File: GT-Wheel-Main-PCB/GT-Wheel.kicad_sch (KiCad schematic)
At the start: 69 parts, among them J2 TC2050, J3 0532610471, J4 USB_A, J5 0532610871, J6 0532610871, U1 STM32F303RETx, U2 USB2512B, U3 AP2112K-3.3, X1 8MHz, X2 24MHz

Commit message: updating PCB
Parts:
- removed C1, C11, C12, C13, C14, C15, C16, C17, C18, C2, C3, C4, C47, C5, C53, C54, C8: 100nF-CER-25V-0402, Capacitor_SMD:C_0402_1005Metric, symbol CAP-SMD-25V:100nF-CER-25V-0402
- removed C10, C9: 10uF-CER-25V-0805, Capacitor_SMD:C_0805_2012Metric, symbol CAP-SMD-25V:10uF-CER-25V-0805
- removed C19, C20: ~, Capacitor_SMD:C_0402_1005Metric, symbol CAP-SMD-50V:18pF-CER-50V-0402
- removed C48, C49, C50, C51: ${SIM.PARAMS}, Capacitor_SMD:C_0805_2012Metric, symbol CAP-SMD-25V:1uF-CER-25V-0805
- removed C52: ${SIM.PARAMS}, Capacitor_SMD:C_0805_2012Metric, symbol CAP-SMD-16V:4.7uF-CER-16V-0805
- removed C55: ${SIM.PARAMS}, Capacitor_SMD:CP_Elec_6.3x5.9, symbol CAP-SMD-25V:100uF-ELEC-50V-RAD6.3Dx6H
- removed C6, C7: ~, Capacitor_SMD:C_0402_1005Metric, symbol CAP-SMD-50V:20pF-CER-50V-0402
- removed J2: TC2050, Connector:Tag-Connect_TC2050-IDC-FP_2x05_P1.27mm_Vertical, symbol CONN-TAG-CONNECT:TC2050
- removed J4: USB_A, CONN-USB:GSB12121RSKHR, symbol Connector:USB_A
- removed R1, R13, R14, R15, R16, R17, R18, R3: 100kR-SMD-100mW-0603, Resistor_SMD:R_0603_1608Metric, symbol RES-SMD-100mW:100kR-SMD-100mW-0603
- removed R19: ${SIM.PARAMS}, Resistor_SMD:R_0603_1608Metric, symbol RES-SMD-100mW:49K9R-SMD-100mW-0603
- removed R2: 10kR-SMD-100mW-0603, Resistor_SMD:R_0603_1608Metric, symbol RES-SMD-100mW:10kR-SMD-100mW-0603
- removed R4: 12kR-SMD-100mW-0603, Resistor_SMD:R_0603_1608Metric, symbol RES-SMD-100mW:12kR-SMD-100mW-0603
- removed U1: STM32F303RETx, Package_QFP:LQFP-64_10x10mm_P0.5mm, symbol MCU_ST_STM32F3:STM32F303RETx
- removed U2: USB2512B, Package_DFN_QFN:QFN-36-1EP_6x6mm_P0.5mm_EP3.7x3.7mm_ThermalVias, symbol IC-SMD-USB-HUB:USB2512B
- removed U3: AP2112K-3.3, Package_TO_SOT_SMD:SOT-23-5, symbol Regulator_Linear:AP2112K-3.3
- removed U4: ~, SOT-SMD:SOT-23-6, symbol IC-SMD-LOAD-SW:AP22653W6-7
- removed X1: 8MHz, Crystal:Crystal_SMD_EuroQuartz_MT-4Pin_3.2x2.5mm, symbol XTAL:XTAL_8MHz_12pF
- removed X2: 24MHz, Crystal:Crystal_SMD_EuroQuartz_MT-4Pin_3.2x2.5mm, symbol XTAL:XTAL_24MHz_6pF
- added U1: ATmega2560-16A, Package_QFP:TQFP-100_14x14mm_P0.5mm, symbol MCU_Microchip_ATmega:ATmega2560-16A
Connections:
- net USB_D+: no longer names the net of L1.2
- net USB_D-: no longer names the net of L1.3
- new net: U1.10 (VCC), U1.31 (VCC), U1.61 (VCC), U1.80 (VCC)
- new net: U1.11 (GND), U1.32 (GND), U1.62 (GND), U1.81 (GND), U1.99 (GND)
- no-connect marks 15 -> 0
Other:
- moved on the sheet: D1, D2, D3, J3, J5, J6, L1, LF1, LF2, WP1, WP10, WP11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

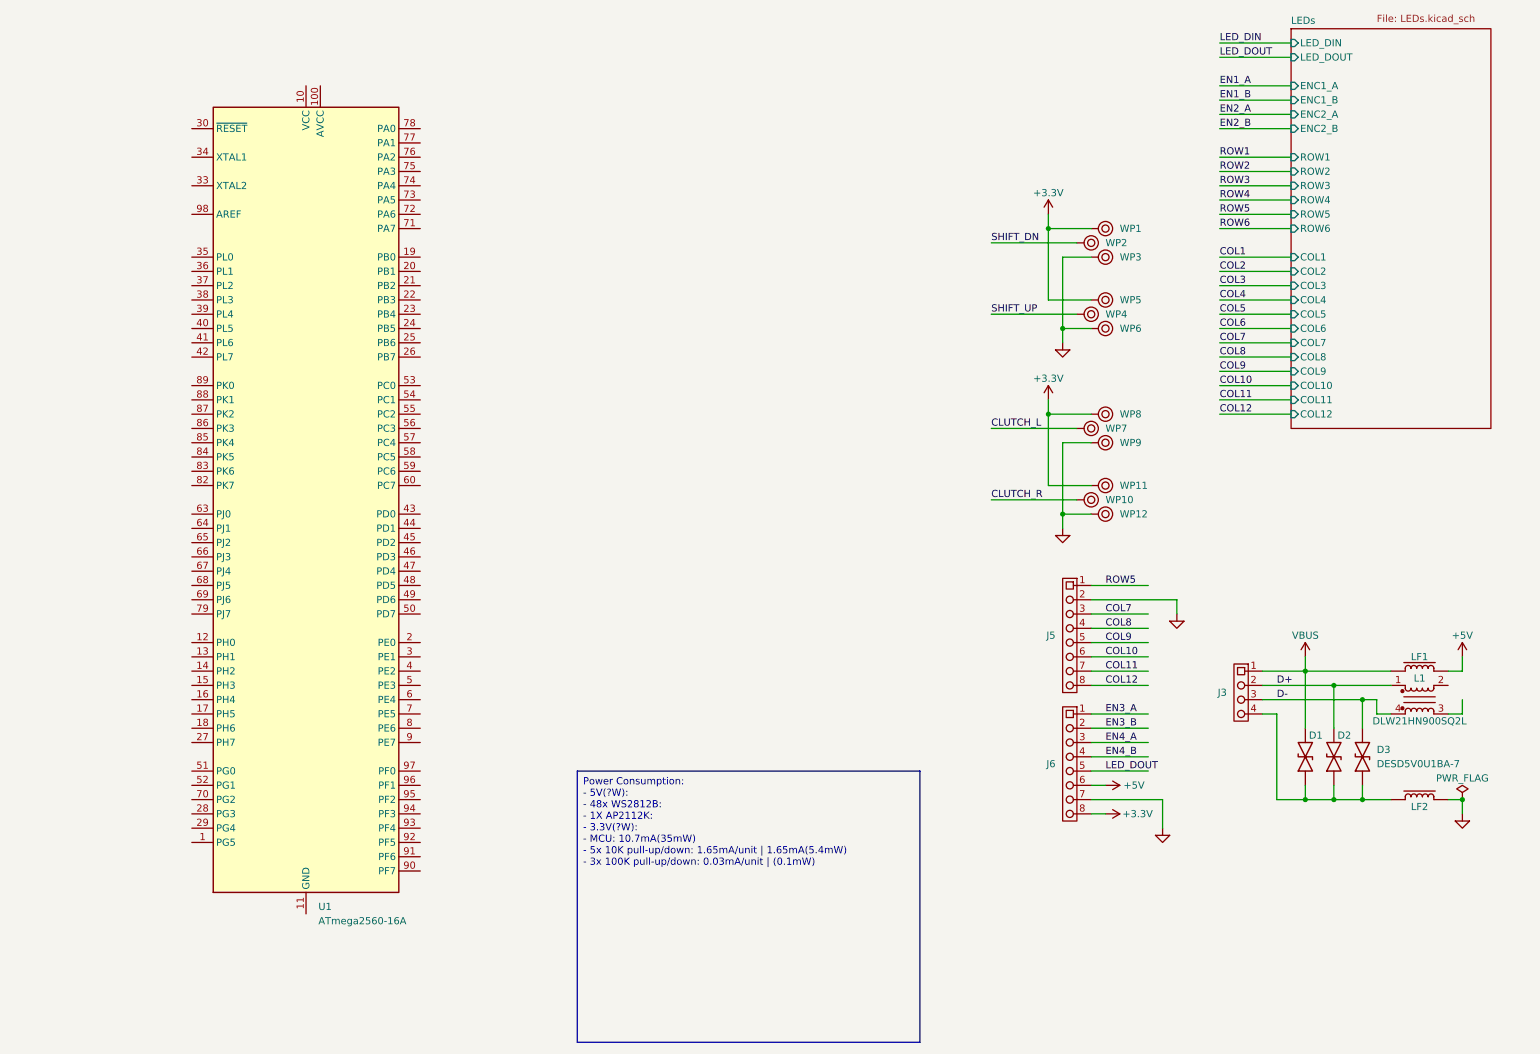
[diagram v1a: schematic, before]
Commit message: reverting to stm32
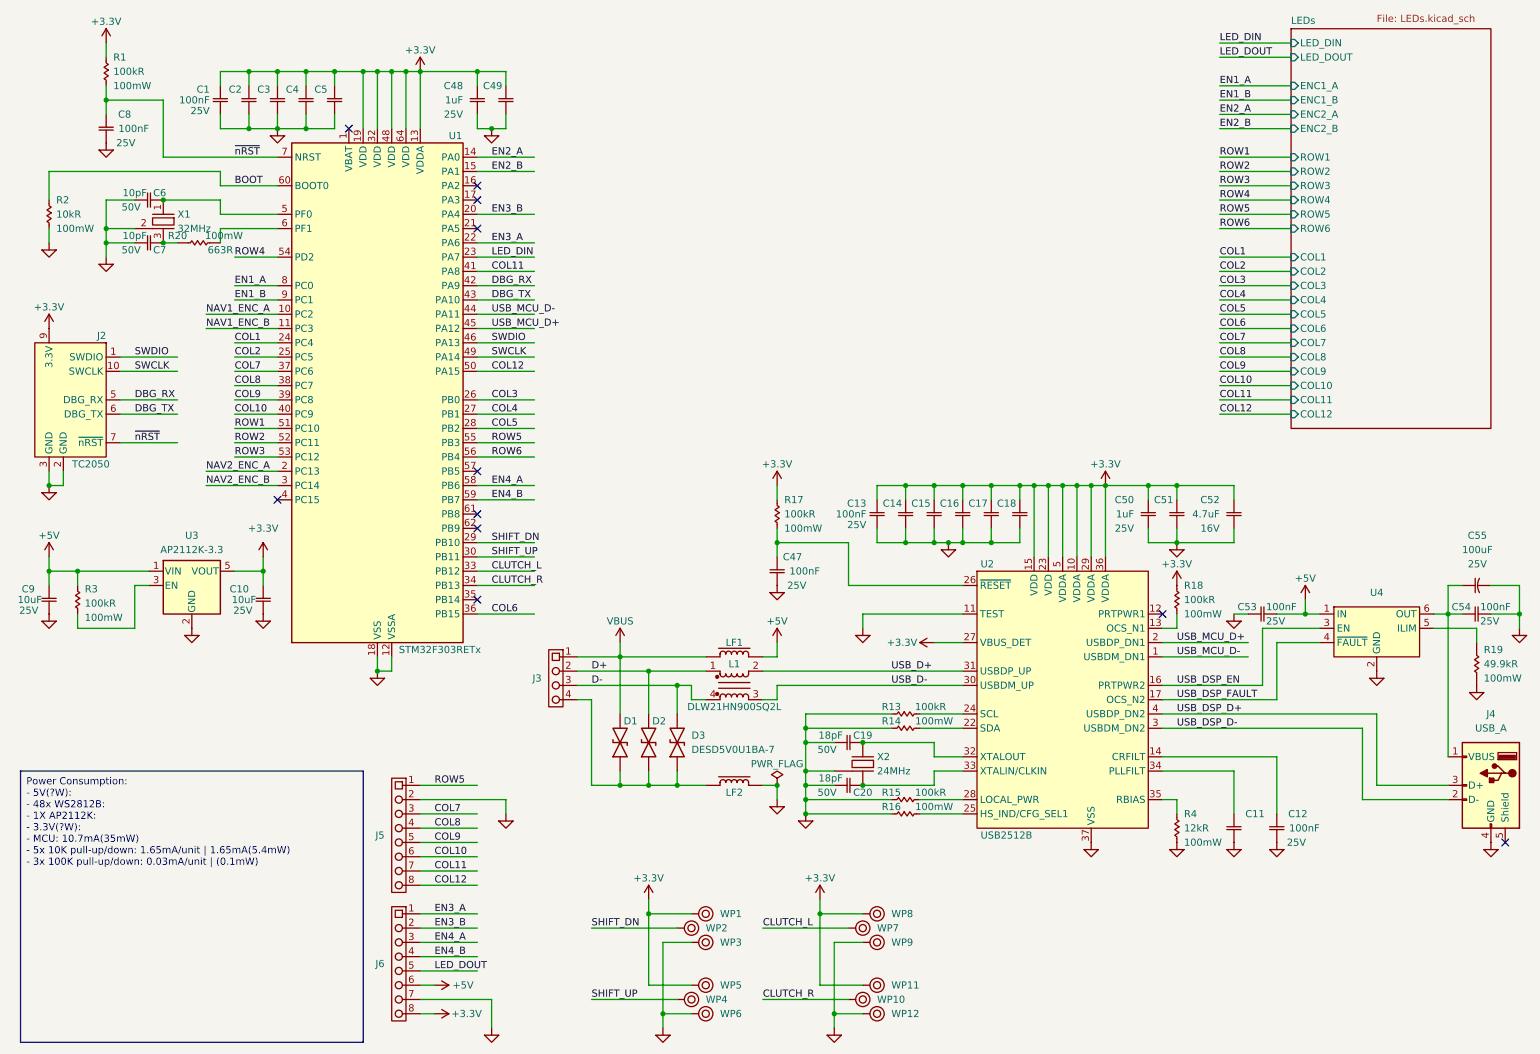
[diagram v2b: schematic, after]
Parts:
- removed U1: ATmega2560-16A, Package_QFP:TQFP-100_14x14mm_P0.5mm, symbol MCU_Microchip_ATmega:ATmega2560-16A
- added C1, C11, C12, C13, C14, C15, C16, C17, C18, C2, C3, C4, C47, C5, C53, C54, C8: 100nF-CER-25V-0402, Capacitor_SMD:C_0402_1005Metric, symbol CAP-SMD-25V:100nF-CER-25V-0402
- added C10, C9: 10uF-CER-25V-0805, Capacitor_SMD:C_0805_2012Metric, symbol CAP-SMD-25V:10uF-CER-25V-0805
- added C19, C20: ~, Capacitor_SMD:C_0402_1005Metric, symbol CAP-SMD-50V:18pF-CER-50V-0402
- added C48, C49, C50, C51: ${SIM.PARAMS}, Capacitor_SMD:C_0805_2012Metric, symbol CAP-SMD-25V:1uF-CER-25V-0805
- added C52: ${SIM.PARAMS}, Capacitor_SMD:C_0805_2012Metric, symbol CAP-SMD-16V:4.7uF-CER-16V-0805
- added C55: ${SIM.PARAMS}, Capacitor_SMD:CP_Elec_6.3x5.9, symbol CAP-SMD-25V:100uF-ELEC-50V-RAD6.3Dx6H
- added C6, C7: ~, Capacitor_SMD:C_0201_0603Metric, symbol CAP-SMD-50V:10pF-CER-50V-0603
- added J2: TC2050, Connector:Tag-Connect_TC2050-IDC-FP_2x05_P1.27mm_Vertical, symbol CONN-TAG-CONNECT:TC2050
- added J4: USB_A, CONN-USB:GSB12121RSKHR, symbol Connector:USB_A
- added R1, R13, R14, R15, R16, R17, R18, R3: 100kR-SMD-100mW-0603, Resistor_SMD:R_0603_1608Metric, symbol RES-SMD-100mW:100kR-SMD-100mW-0603
- added R19: ${SIM.PARAMS}, Resistor_SMD:R_0603_1608Metric, symbol RES-SMD-100mW:49K9R-SMD-100mW-0603
- added R2: 10kR-SMD-100mW-0603, Resistor_SMD:R_0603_1608Metric, symbol RES-SMD-100mW:10kR-SMD-100mW-0603
- added R20: ${SIM.PARAMS}, Resistor_SMD:R_0603_1608Metric, symbol RES-SMD-100mW:663R-SMD-100mW-0603
- added R4: 12kR-SMD-100mW-0603, Resistor_SMD:R_0603_1608Metric, symbol RES-SMD-100mW:12kR-SMD-100mW-0603
- added U1: STM32F303RETx, Package_QFP:LQFP-64_10x10mm_P0.5mm, symbol MCU_ST_STM32F3:STM32F303RETx
- added U2: USB2512B, Package_DFN_QFN:QFN-36-1EP_6x6mm_P0.5mm_EP3.7x3.7mm_ThermalVias, symbol IC-SMD-USB-HUB:USB2512B
- added U3: AP2112K-3.3, Package_TO_SOT_SMD:SOT-23-5, symbol Regulator_Linear:AP2112K-3.3
- added U4: ~, SOT-SMD:SOT-23-6, symbol IC-SMD-LOAD-SW:AP22653W6-7
- added X1: 32MHz, Crystal:Crystal_SMD_EuroQuartz_X22-4Pin_2.5x2.0mm, symbol XTAL:XTAL_32MHz_10pF
- added X2: 24MHz, Crystal:Crystal_SMD_EuroQuartz_MT-4Pin_3.2x2.5mm, symbol XTAL:XTAL_24MHz_6pF
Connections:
- net CLUTCH_L: now also U1.33 (PB12)
- net CLUTCH_R: now also U1.34 (PB13)
- net COL1: now also U1.24 (PC4)
- net COL10: now also U1.40 (PC9)
- net COL11: now also U1.41 (PA8)
- net COL12: now also U1.50 (PA15)
- net COL2: now also U1.25 (PC5)
- net COL3: now also U1.26 (PB0)
- net COL4: now also U1.27 (PB1)
- net COL5: now also U1.28 (PB2)
- net COL6: now also U1.36 (PB15)
- net COL7: now also U1.37 (PC6)
- net COL8: now also U1.38 (PC7)
- net COL9: now also U1.39 (PC8)
- net EN1_A: now also U1.8 (PC0)
- net EN1_B: now also U1.9 (PC1)
- net EN2_A: now also U1.14 (PA0)
- net EN2_B: now also U1.15 (PA1)
- net EN3_A: now also U1.22 (PA6)
- net EN3_B: now also U1.20 (PA4)
- net EN4_A: now also U1.58 (PB6)
- net EN4_B: now also U1.59 (PB7)
- net LED_DIN: now also U1.23 (PA7)
- net LOGIC_GND: now also C1.2, C10.2, C11.2, C12.2, C13.2, C14.2, C15.2, C16.2, C17.2, C18.2, C19.1, C2.2, C20.1, C3.2, C4.2, C47.2, C48.2, C49.2, C5.2, C50.2, C51.2, C52.2, C53.1, C54.2, C55.2, C6.1, C7.1, C8.2, C9.2, J2.2 (GND), J2.3 (GND), J4.4 (GND), R13.1, R14.1, R15.1, R16.1, R19.2, R2.2, R4.2, U1.12 (VSSA), U1.18 (VSS), U1.31 (VSS), U1.47 (VSS), U1.63 (VSS), U2.11 (TEST), U2.37 (VSS), U3.2 (GND), U4.2 (GND), X1.2, X1.4, X2.2, X2.4
- net ROW1: now also U1.51 (PC10)
- net ROW2: now also U1.52 (PC11)
- net ROW3: now also U1.53 (PC12)
- net ROW4: now also U1.54 (PD2)
- net ROW5: now also U1.55 (PB3)
- net ROW6: now also U1.56 (PB4)
- net SHIFT_DN: now also U1.29 (PB10)
- net SHIFT_UP: now also U1.30 (PB11)
- net USB_D+: now reaches L1.2
- net USB_D+: now also U2.31 (USBDP_UP)
- net USB_D-: now reaches L1.3
- net USB_D-: now also U2.30 (USBDM_UP)
- new net: C54.1, C55.1, J4.1 (VBUS), U4.6 (OUT)
- new net: C9.1, R3.1, U3.1 (VIN)
- new net: R3.2, U3.3 (EN)
- new net: C13.1, C14.1, C15.1, C16.1, C17.1, C18.1, C50.1, C51.1, C52.1, U2.10 (VDDA), U2.15 (VDD), U2.23 (VDD), U2.29 (VDDA), U2.36 (VDDA), U2.5 (VDDA)
- new net: C1.1, C2.1, C3.1, C4.1, C48.1, C49.1, C5.1, U1.13 (VDDA), U1.19 (VDD), U1.32 (VDD), U1.48 (VDD), U1.64 (VDD)
- new net: C53.2, U4.1 (IN)
- new net: R19.1, U4.5 (ILIM)
- new net: C6.2, U1.5 (PF0), X1.1
- new net: R20.2, U1.6 (PF1)
- new net: C47.1, R17.2, U2.26 (~{RESET})
- new net: C19.2, U2.32 (XTALOUT), X2.1
- new net: C7.2, R20.1, X1.3
- new net: R18.2, U2.13 (OCS_N1)
- new net: C20.2, U2.33 (XTALIN/CLKIN), X2.3
- new net: R13.2, U2.24 (SCL)
- new net: C12.1, U2.14 (CRFILT)
- new net: R14.2, U2.22 (SDA)
- new net: R16.2, U2.25 (HS_IND/CFG_SEL1)
- new net: R15.2, U2.28 (LOCAL_PWR)
- new net: C11.1, U2.34 (PLLFILT)
- new net: R4.1, U2.35 (RBIAS)
- new net +3.3V: C10.1, U3.5 (VOUT)
- new net BOOT: R2.1, U1.60 (BOOT0)
- new net DBG_RX: J2.5 (DBG_RX), U1.42 (PA9)
- new net DBG_TX: J2.6 (DBG_TX), U1.43 (PA10)
- new net NAV1_ENC_A: U1.10 (PC2)
- new net NAV1_ENC_B: U1.11 (PC3)
- new net NAV2_ENC_A: U1.2 (PC13)
- new net NAV2_ENC_B: U1.3 (PC14)
- new net SWCLK: J2.10 (SWCLK), U1.49 (PA14)
- new net SWDIO: J2.1 (SWDIO), U1.46 (PA13)
- new net USB_DSP_D+: J4.3 (D+), U2.4 (USBDP_DN2)
- new net USB_DSP_D-: J4.2 (D-), U2.3 (USBDM_DN2)
- new net USB_DSP_EN: U2.16 (PRTPWR2), U4.3 (EN)
- new net USB_DSP_FAULT: U2.17 (OCS_N2), U4.4 (~{FAULT})
- new net USB_MCU_D+: U1.45 (PA12), U2.2 (USBDP_DN1)
- new net USB_MCU_D-: U1.44 (PA11), U2.1 (USBDM_DN1)
- new net ~{nRST}: C8.1, J2.7 (~{nRST}), R1.2, U1.7 (NRST)
- no-connect marks 0 -> 11
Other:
- moved on the sheet: D1, D2, D3, J3, J5, J6, L1, LF1, LF2, WP1, WP10, WP11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

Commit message: removing usb hub
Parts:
- removed C11, C12, C13, C14, C15, C16, C17, C18, C47, C53, C54: 100nF-CER-25V-0402, Capacitor_SMD:C_0402_1005Metric, symbol CAP-SMD-25V:100nF-CER-25V-0402
- removed C19, C20: ~, Capacitor_SMD:C_0402_1005Metric, symbol CAP-SMD-50V:18pF-CER-50V-0402
- removed C50, C51: ${SIM.PARAMS}, Capacitor_SMD:C_0805_2012Metric, symbol CAP-SMD-25V:1uF-CER-25V-0805
- removed C52: ${SIM.PARAMS}, Capacitor_SMD:C_0805_2012Metric, symbol CAP-SMD-16V:4.7uF-CER-16V-0805
- removed C55: ${SIM.PARAMS}, Capacitor_SMD:CP_Elec_6.3x5.9, symbol CAP-SMD-25V:100uF-ELEC-50V-RAD6.3Dx6H
- removed J4: USB_A, CONN-USB:GSB12121RSKHR, symbol Connector:USB_A
- removed R13, R14, R15, R16, R17, R18: 100kR-SMD-100mW-0603, Resistor_SMD:R_0603_1608Metric, symbol RES-SMD-100mW:100kR-SMD-100mW-0603
- removed R19: ${SIM.PARAMS}, Resistor_SMD:R_0603_1608Metric, symbol RES-SMD-100mW:49K9R-SMD-100mW-0603
- removed R4: 12kR-SMD-100mW-0603, Resistor_SMD:R_0603_1608Metric, symbol RES-SMD-100mW:12kR-SMD-100mW-0603
- removed U2: USB2512B, Package_DFN_QFN:QFN-36-1EP_6x6mm_P0.5mm_EP3.7x3.7mm_ThermalVias, symbol IC-SMD-USB-HUB:USB2512B
- removed U4: ~, SOT-SMD:SOT-23-6, symbol IC-SMD-LOAD-SW:AP22653W6-7
- removed X2: 24MHz, Crystal:Crystal_SMD_EuroQuartz_MT-4Pin_3.2x2.5mm, symbol XTAL:XTAL_24MHz_6pF
- added C64, C65, C66, C67: 100nF-CER-25V-0402, Capacitor_SMD:C_0402_1005Metric, symbol CAP-SMD-25V:100nF-CER-25V-0402
- added D14 (x2): BAT43W-TP, Diode_SMD:D_SOD-123, symbol DIODE-SMD-SCHOTTKY:BAT43W-TP
- added R37, R38, R39, R40, R41, R42, R43, R44: 10kR-SMD-100mW-0603, Resistor_SMD:R_0603_1608Metric, symbol RES-SMD-100mW:10kR-SMD-100mW-0603
- added SW7, SW8: ~, SWITCH-THT-FUNKY:RKJXT1F42001, symbol SWITCH-THT-FUNKY:RKJXT1F42001
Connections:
- net USB_D+ is gone; now on net USB_MCU_D+: L1.2
- net USB_D- is gone; now on net USB_MCU_D-: L1.3
- net COL1: now also J5.5, SW7.1 (A), SW8.1 (A)
- net COL2: now also J5.6, SW7.2 (B), SW8.2 (B)
- net COL3: now also J5.7, U1.37 (PC6), SW7.3 (C), SW8.3 (C); no longer U1.26 (PB0)
- net COL4: now also U1.38 (PC7), SW7.4 (D), SW8.4 (D); no longer U1.27 (PB1)
- net LOGIC_GND: now also J5.4, J5.8, C64.2, C65.2, C66.2, C67.2, SW7.10 (GND), SW7.9 (ENC_C), SW8.10 (GND), SW8.9 (ENC_C); no longer J5.2
- net NAV1_ENC_A: now also C65.1, R37.1
- net NAV1_ENC_B: now also C64.1, R38.1
- net NAV2_ENC_A: now also C67.1, R41.1
- net NAV2_ENC_B: now also C66.1, R42.1
- net ROW1: now also U1.39 (PC8); no longer U1.51 (PC10)
- net ROW2: now also U1.40 (PC9); no longer U1.52 (PC11)
- net ROW3: now also U1.51 (PC10); no longer U1.53 (PC12)
- net ROW4: now also J5.2, U1.52 (PC11)
- net ROW5: now also J5.3, U1.53 (PC12); no longer J5.1, U1.55 (PB3)
- net ROW6: now also U1.26 (PB0), D14.2 (A); no longer U1.56 (PB4)
- net EN8_A: now reaches U1.35 (PB14)
- net EN6_B: now reaches U1.57 (PB5)
- net EN7_A: now reaches U1.61 (PB8)
- net EN7_B: now reaches U1.62 (PB9)
- removed net COL10: J5.6, U1.40 (PC9)
- net COL11: no longer names the net of U1.41 (PA8)
- net COL11: no longer J5.7
- net COL12: no longer names the net of U1.50 (PA15)
- net COL12: no longer J5.8
- net COL5 renamed EN5_A
- net COL6 renamed EN8_B
- removed net COL7: J5.3, U1.37 (PC6)
- removed net COL8: J5.4, U1.38 (PC7)
- removed net COL9: J5.5, U1.39 (PC8)
- new net: R39.1, R40.1
- new net: R38.2, R39.2, SW7.8 (ENC_B)
- new net: R42.2, R43.2, SW8.8 (ENC_B)
- new net: R37.2, R40.2, SW7.7 (ENC_A)
- new net: R41.2, R44.2, SW8.7 (ENC_A)
- new net: R43.1, R44.1
- new net: D14.1 (K), SW8.6 (COM)
- new net: D14.1 (K), SW7.6 (COM)
- new net EN5_B: U1.55 (PB3)
- new net EN6_A: U1.56 (PB4)
- new net ROW7: D14.2 (A), U1.27 (PB1)
- no-connect marks 11 -> 9
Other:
- sheet LEDs ports: added ENC5_A, ENC5_B, ENC6_A, ENC6_B, ENC7_A, ENC7_B, ENC8_A, ENC8_B; removed COL10, COL11, COL12, COL5, COL6, COL7, COL8, COL9, ROW4, ROW5, ROW6
